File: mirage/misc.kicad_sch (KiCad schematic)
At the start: 1 part

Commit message: feat: initialize structure
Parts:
- removed LED1: 17-21SUYC/TR8, EasyEDA:LED0805-R-RD, symbol EasyEDA:17-21SUYC_TR8
- added D1: LED Yellow, LED_SMD:LED_0603_1608Metric, symbol Device:LED
- added H1, H2, H3, H4: MountingHole, MountingHole:MountingHole_3.2mm_M3, symbol Mechanical:MountingHole
- added R1: 1K0R, Resistor_SMD:R_0402_1005Metric, symbol Device:R
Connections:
- net YELLOW_LED: now also D1.2 (A)
- new net: D1.1 (K), R1.1
- new net GND: R1.2

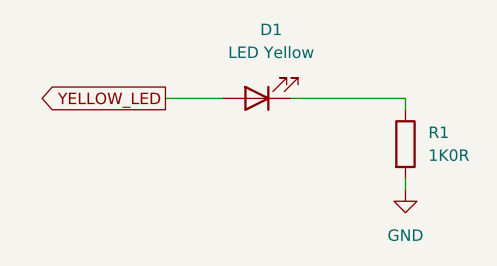
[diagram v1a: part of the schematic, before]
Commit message: feat(sensor): fundamental sensor lists
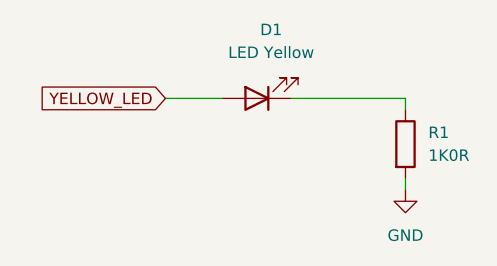
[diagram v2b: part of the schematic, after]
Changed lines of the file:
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@@
 	)
 	(global_label "YELLOW_LED"
-		(shape output)
+		(shape input)
 		(at 45.72 35.56 180)
 		(fields_autoplaced yes)

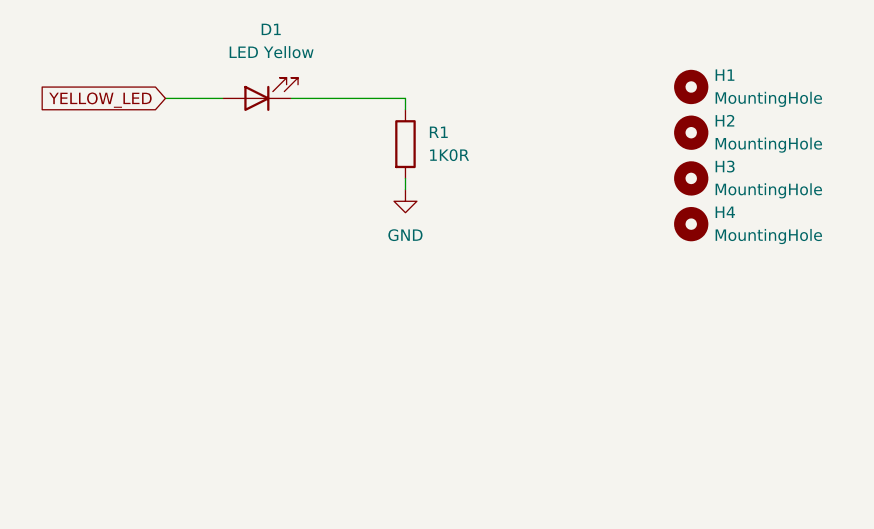
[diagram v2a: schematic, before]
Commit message: feat: add red LED
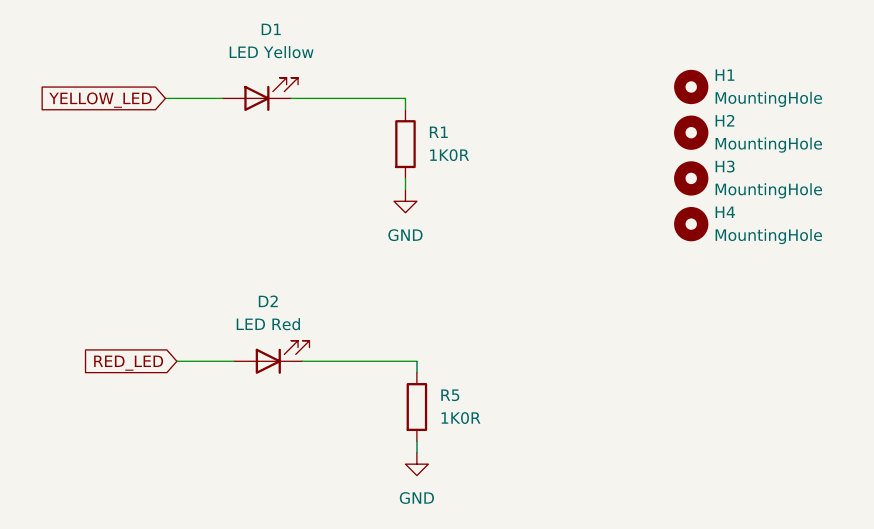
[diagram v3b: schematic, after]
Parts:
- added D2: LED Red, LED_SMD:LED_0603_1608Metric, symbol Device:LED
- added R5: 1K0R, Resistor_SMD:R_0402_1005Metric, symbol Device:R
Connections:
- net GND: now also R5.2
- new net: D2.1 (K), R5.1
- new net RED_LED: D2.2 (A)
